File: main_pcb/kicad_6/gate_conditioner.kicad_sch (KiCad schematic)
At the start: 8 parts, among them Q901 MMBT3904, Q902 MMBT3904

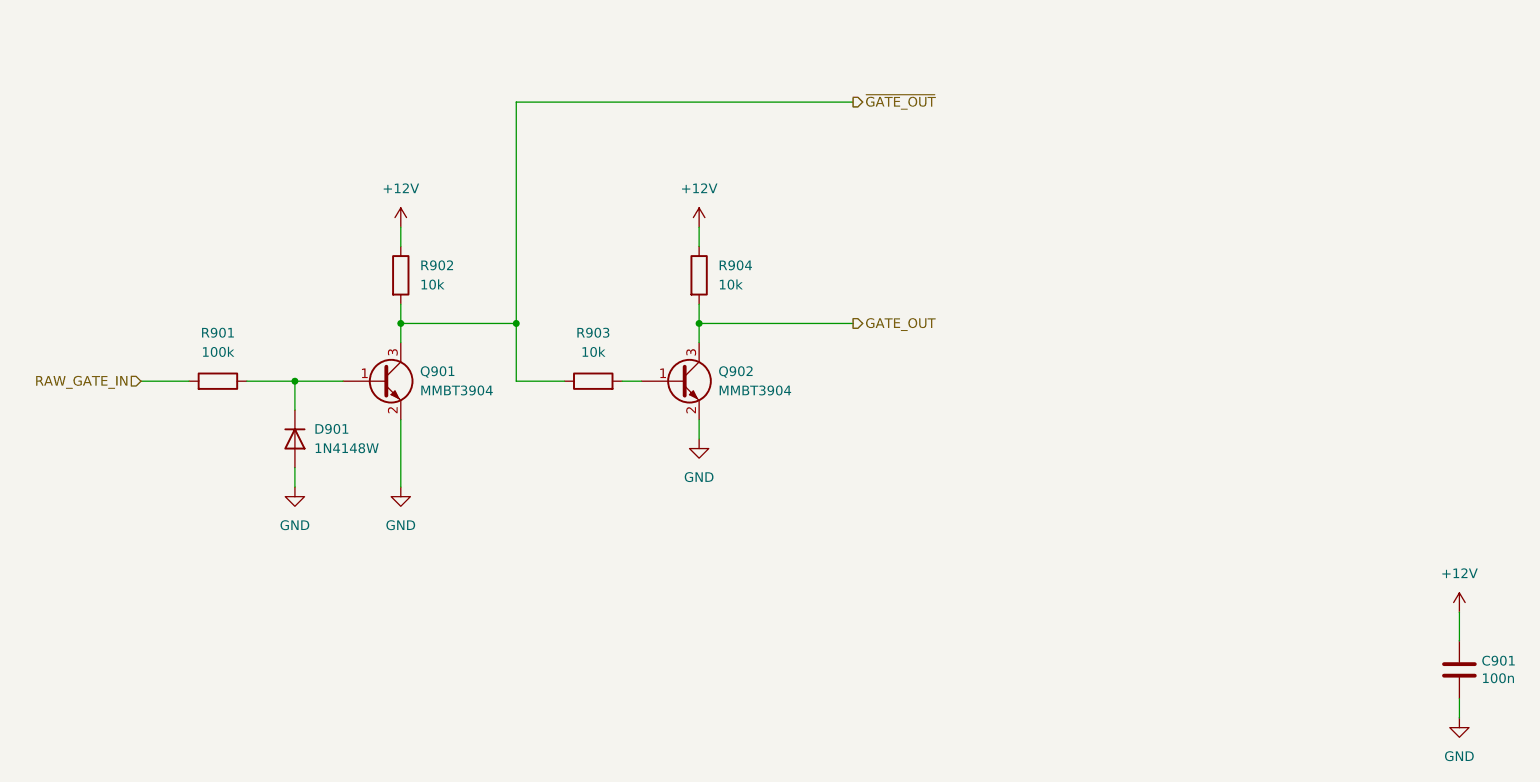
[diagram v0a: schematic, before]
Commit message: Update rev 0.1, fix VCA tails, add local 2v5 regs, change some pot footprints
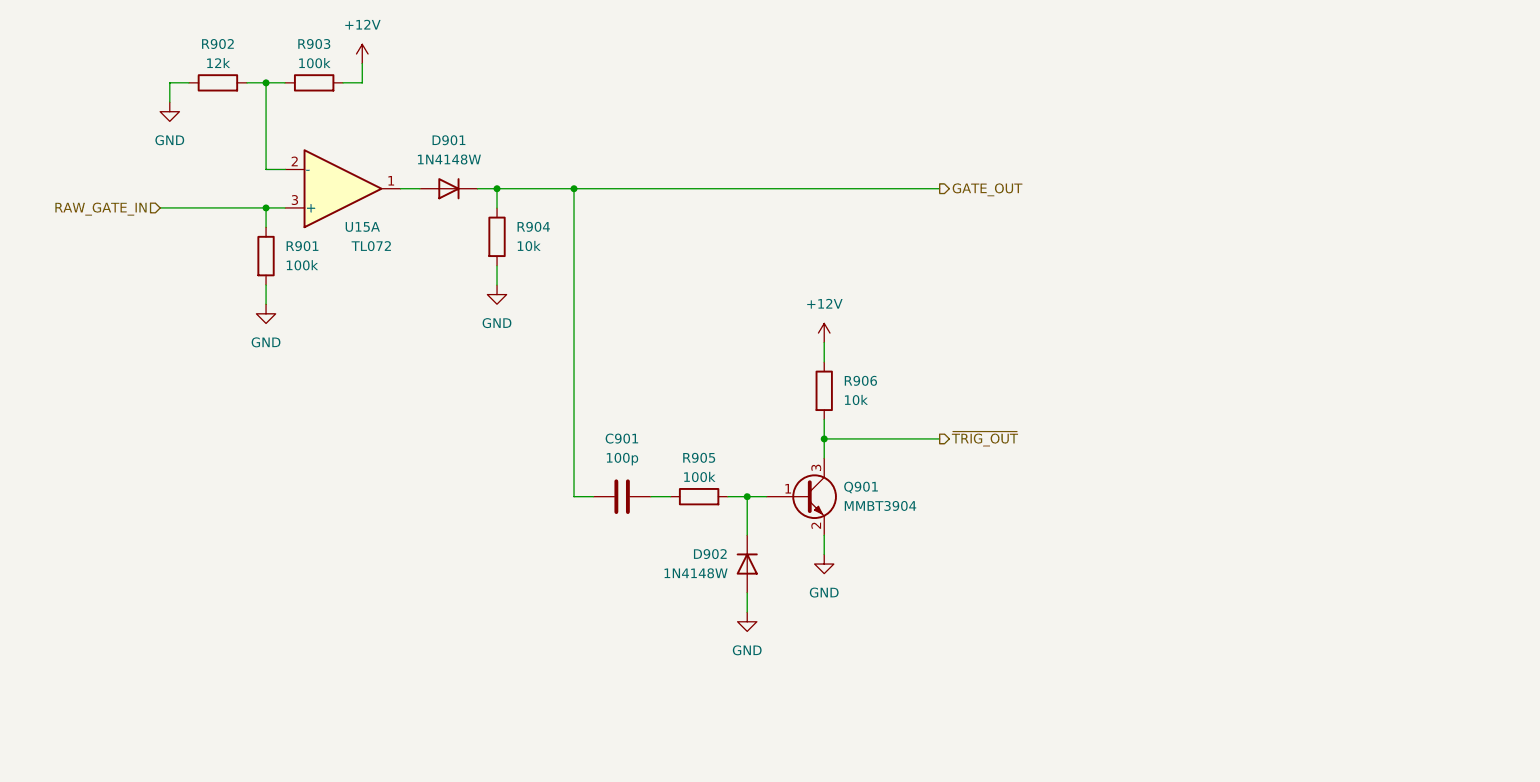
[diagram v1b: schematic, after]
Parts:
- removed Q902: MMBT3904, Package_TO_SOT_SMD:SOT-23, symbol Transistor_BJT:MMBT3904
- added D902: 1N4148W, Diode_SMD:D_SOD-123, symbol Diode:1N4148W
- added R905: 100k, Resistor_SMD:R_0603_1608Metric, symbol Device:R
- added R906: 10k, Resistor_SMD:R_0603_1608Metric, symbol Device:R
- added U15: TL072, Package_SO:SOIC-8_3.9x4.9mm_P1.27mm, symbol Amplifier_Operational:TL072
- C901: value 100n -> 100p
- R902: value 10k -> 12k
- R903: value 10k -> 100k
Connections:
- net +12V: now also R903.2, R906.1; no longer C901.1, R902.1, R904.1
- net GATE_OUT: now also C901.1, D901.1 (K), R904.1; no longer R904.2
- net GND: now also R901.2, R902.1, R904.2, D902.2 (A); no longer C901.2, D901.2 (A)
- net RAW_GATE_IN: now also R901.1, U15.3 (+); no longer R901.2
- net ~{GATE_OUT}: no longer names the net of R902.2, R903.1
- net ~{GATE_OUT}: now also U15.2 (-); no longer Q901.3 (C)
- new net: D902.1 (K), Q901.1 (B), R905.2
- new net: C901.2, R905.1
- new net: D901.2 (A), U15.1
- new net ~{TRIG_OUT}: Q901.3 (C), R906.2
